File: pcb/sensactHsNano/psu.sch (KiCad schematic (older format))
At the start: 12 parts, among them U7 TPS5430DDA

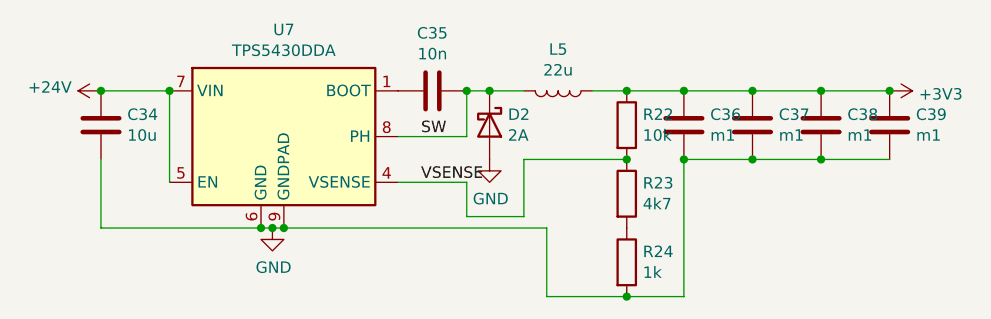
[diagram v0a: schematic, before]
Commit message: sensactUP2, sensactHsNano sensactHsLED sensactOutdoor as ordered at JLCPCB
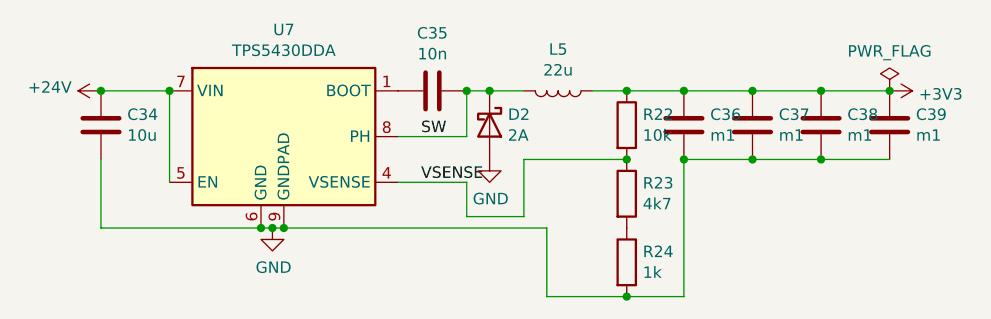
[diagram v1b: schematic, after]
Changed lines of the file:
@@
 Text Label 3350 1700 0    50   ~ 0
 VSENSE
+$Comp
+L power:PWR_FLAG #FLG0105
+U 1 1 60F7D59C
+P 5400 1300
+F 0 "#FLG0105" H 5400 1375 50  0001 C CNN
+F 1 "PWR_FLAG" H 5400 1473 50  0000 C CNN
+F 2 "" H 5400 1300 50  0001 C CNN
+F 3 "~" H 5400 1300 50  0001 C CNN
+	1    5400 1300
+	1    0    0    -1
+$EndComp
 $EndSCHEMATC

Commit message: sensactHsNano for Reflow Soldering
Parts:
- C34, C36, C37, C38, C39: footprint Capacitor_SMD:C_1210_3225Metric_Pad1.33x2.70mm_HandSolder -> Capacitor_SMD:C_1206_3216Metric
- C35: footprint Capacitor_SMD:C_0805_2012Metric_Pad1.18x1.45mm_HandSolder -> Capacitor_SMD:C_0805_2012Metric
- D2: footprint Diode_SMD:D_SMB_Handsoldering -> Diode_SMD:D_SMB
- L5: footprint liebler_PASSIVES:Inductor_CDRH104_handsolder -> liebler_PASSIVES:L_1040
- R22, R23, R24: footprint Resistor_SMD:R_0805_2012Metric_Pad1.20x1.40mm_HandSolder -> Resistor_SMD:R_0603_1608Metric
- U7: footprint sensact:SOIC-8_3.9x4.9mm_Pitch1.27mm_pad_handsolder -> Package_SO:TI_SO-PowerPAD-8_ThermalVias
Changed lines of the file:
@@
 F 0 "U7" H 2750 1967 50  0000 C CNN
 F 1 "TPS5430DDA" H 2750 1876 50  0000 C CNN
-F 2 "sensact:SOIC-8_3.9x4.9mm_Pitch1.27mm_pad_handsolder" H 2800 1150 50  0001 L CIN
+F 2 "Package_SO:TI_SO-PowerPAD-8_ThermalVias" H 2800 1150 50  0001 L CIN
 F 3 "http://www.ti.com/lit/ds/symlink/tps5430.pdf" H 2750 1500 50  0001 C CNN
 	1    2750 1500
@@
 F 0 "C35" V 3148 1300 50  0000 C CNN
 F 1 "10n" V 3239 1300 50  0000 C CNN
-F 2 "Capacitor_SMD:C_0805_2012Metric_Pad1.18x1.45mm_HandSolder" H 3438 1150 50  0001 C CNN
+F 2 "Capacitor_SMD:C_0805_2012Metric" H 3438 1150 50  0001 C CNN
 F 3 "~" H 3400 1300 50  0001 C CNN
 	1    3400 1300
@@
 F 0 "D2" V 3604 1530 50  0000 L CNN
 F 1 "2A" V 3695 1530 50  0000 L CNN
-F 2 "Diode_SMD:D_SMB_Handsoldering" H 3650 1450 50  0001 C CNN
+F 2 "Diode_SMD:D_SMB" H 3650 1450 50  0001 C CNN
 F 3 "~" H 3650 1450 50  0001 C CNN
 	1    3650 1450
@@
 F 0 "L5" V 3769 1300 50  0000 C CNN
 F 1 "22u" V 3860 1300 50  0000 C CNN
-F 2 "liebler_PASSIVES:Inductor_CDRH104_handsolder" H 3950 1300 50  0001 C CNN
+F 2 "liebler_PASSIVES:L_1040" H 3950 1300 50  0001 C CNN
 F 3 "~" H 3950 1300 50  0001 C CNN
 	1    3950 1300
@@
 F 0 "C36" H 4615 1496 50  0000 L CNN
 F 1 "m1" H 4615 1405 50  0000 L CNN
-F 2 "Capacitor_SMD:C_1210_3225Metric_Pad1.33x2.70mm_HandSolder" H 4538 1300 50  0001 C CNN
+F 2 "Capacitor_SMD:C_1206_3216Metric" H 4538 1300 50  0001 C CNN
 F 3 "~" H 4500 1450 50  0001 C CNN
 	1    4500 1450
@@
 F 0 "C37" H 4915 1496 50  0000 L CNN
 F 1 "m1" H 4915 1405 50  0000 L CNN
-F 2 "Capacitor_SMD:C_1210_3225Metric_Pad1.33x2.70mm_HandSolder" H 4838 1300 50  0001 C CNN
+F 2 "Capacitor_SMD:C_1206_3216Metric" H 4838 1300 50  0001 C CNN
 F 3 "~" H 4800 1450 50  0001 C CNN
 	1    4800 1450
@@
 F 0 "C38" H 5215 1496 50  0000 L CNN
 F 1 "m1" H 5215 1405 50  0000 L CNN
-F 2 "Capacitor_SMD:C_1210_3225Metric_Pad1.33x2.70mm_HandSolder" H 5138 1300 50  0001 C CNN
+F 2 "Capacitor_SMD:C_1206_3216Metric" H 5138 1300 50  0001 C CNN
 F 3 "~" H 5100 1450 50  0001 C CNN
 	1    5100 1450
@@
 F 0 "C39" H 5515 1496 50  0000 L CNN
 F 1 "m1" H 5515 1405 50  0000 L CNN
-F 2 "Capacitor_SMD:C_1210_3225Metric_Pad1.33x2.70mm_HandSolder" H 5438 1300 50  0001 C CNN
+F 2 "Capacitor_SMD:C_1206_3216Metric" H 5438 1300 50  0001 C CNN
 F 3 "~" H 5400 1450 50  0001 C CNN
 	1    5400 1450
@@
 F 0 "R22" H 4320 1496 50  0000 L CNN
 F 1 "10k" H 4320 1405 50  0000 L CNN
-F 2 "Resistor_SMD:R_0805_2012Metric_Pad1.20x1.40mm_HandSolder" V 4180 1450 50  0001 C CNN
+F 2 "Resistor_SMD:R_0603_1608Metric" V 4180 1450 50  0001 C CNN
 F 3 "~" H 4250 1450 50  0001 C CNN
 	1    4250 1450
@@
 F 0 "R23" H 4320 1796 50  0000 L CNN
 F 1 "4k7" H 4320 1705 50  0000 L CNN
-F 2 "Resistor_SMD:R_0805_2012Metric_Pad1.20x1.40mm_HandSolder" V 4180 1750 50  0001 C CNN
+F 2 "Resistor_SMD:R_0603_1608Metric" V 4180 1750 50  0001 C CNN
 F 3 "~" H 4250 1750 50  0001 C CNN
 	1    4250 1750
@@
 F 0 "C34" H 2065 1496 50  0000 L CNN
 F 1 "10u" H 2065 1405 50  0000 L CNN
-F 2 "Capacitor_SMD:C_1210_3225Metric_Pad1.33x2.70mm_HandSolder" H 1988 1300 50  0001 C CNN
+F 2 "Capacitor_SMD:C_1206_3216Metric" H 1988 1300 50  0001 C CNN
 F 3 "~" H 1950 1450 50  0001 C CNN
 	1    1950 1450
@@
 F 0 "R24" H 4320 2096 50  0000 L CNN
 F 1 "1k" H 4320 2005 50  0000 L CNN
-F 2 "Resistor_SMD:R_0805_2012Metric_Pad1.20x1.40mm_HandSolder" V 4180 2050 50  0001 C CNN
+F 2 "Resistor_SMD:R_0603_1608Metric" V 4180 2050 50  0001 C CNN
 F 3 "~" H 4250 2050 50  0001 C CNN
 	1    4250 2050
